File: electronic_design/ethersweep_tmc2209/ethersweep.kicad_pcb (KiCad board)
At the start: 2 copper layers, 79 x 38 mm, 111 parts, among them J1 AVR-ISP-6, J10 HR911105A, J12 USB_C_Receptacle_USB2.0, J2 Conn_01x02_Male, J3 Conn_01x04_Female, J4 Conn_01x03_Male, J5 Conn_01x03_Male, J6 Conn_01x06_Female, J7 Conn_01x06_Male, J8 AVR-ISP-6, J9 Conn_01x04_Female, SW1 SW_Push, U3 STM32F103C8Tx, U4 DD4012SA, U5 AS5600, U6 W5500, U7 TMC2209-LA, Y2 Crystal_25MHz, Y3 Crystal

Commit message: minor design changes
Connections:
- U3 pad 11: voltage_detect -> RST_ETHERNET
- U3 pad 19: RST_ETHERNET -> voltage_detect
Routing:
- net ETH_INT: track 45.0 -> 47.3 mm
- net voltage_detect: track 15.6 -> 13.7 mm
- net +3V3: track 248.8 -> 250.2 mm
- net rst: track 38.6 -> 39.8 mm
- net ESTOP: track 53.3 -> 52.6 mm
- net MOT_UART_RX: track 35.6 -> 34.8 mm
- net RST_ETHERNET: track 46.1 -> 46.7 mm
- net SCK: track 53.3 -> 53.9 mm
- net GND: vias 217 -> 252
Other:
- board text added: "ETHERSWEEP 2023-01-14"
- board text removed: "ETHERSWEEP 2023-01-10"

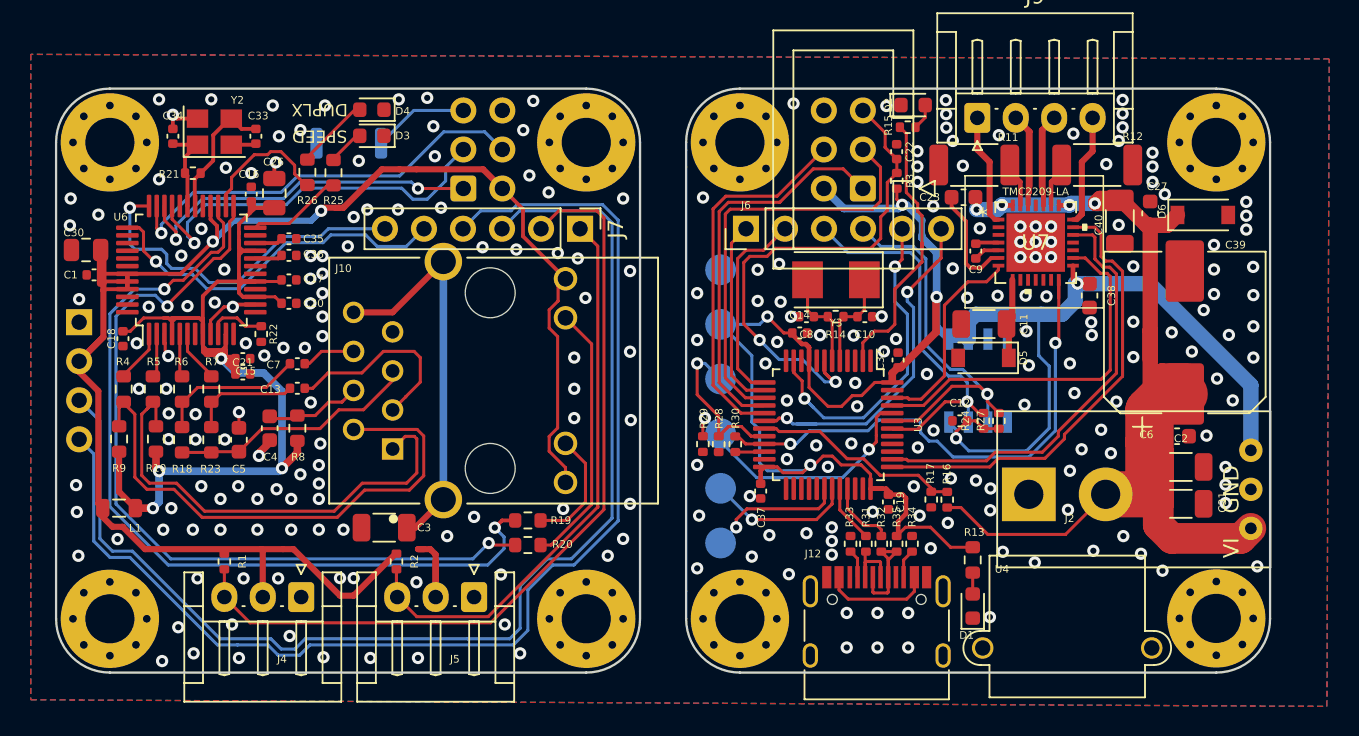
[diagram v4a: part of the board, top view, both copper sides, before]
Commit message: pcb design changes, reorganisation, JLC part number assignments, size corrections
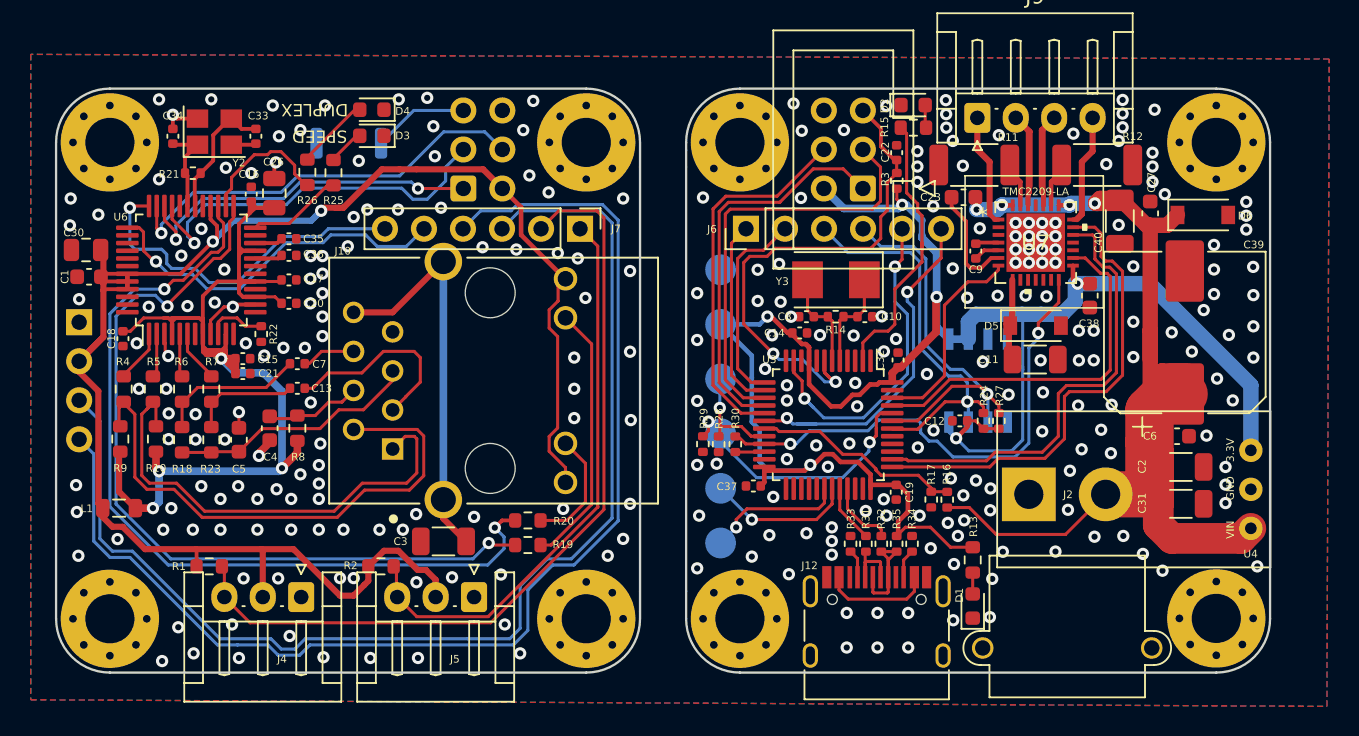
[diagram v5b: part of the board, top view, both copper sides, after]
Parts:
- C1: footprint Capacitor_SMD:C_0402_1005Metric -> Capacitor_SMD:C_0603_1608Metric
- R1, R15, R2: footprint Resistor_SMD:R_0402_1005Metric -> Resistor_SMD:R_0603_1608Metric
- moved C11 4.06 mm to (209.8, 44.3), turned to 0 degrees
- moved D5 3.98 mm to (209.8, 42.1), turned to 0 degrees
- moved C3 3.96 mm to (171.3, 56.2)
- moved R2 1.06 mm to (167.2, 57.8), turned to 0 degrees
- moved R1 1.03 mm to (156.1, 57.8), turned to 0 degrees
- moved C19 0.81 mm to (200.8, 53.0)
- moved C37 0.58 mm to (191.5, 52.6), turned to 180 degrees
- moved R15 0.37 mm to (201.9, 29.2)
- moved C1 0.35 mm to (148.2, 38.9)
- moved R9 0.08 mm to (150.3, 49.5)
- moved C22 0.07 mm to (200.8, 30.9)
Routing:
- net BOOT_1: track 11.3 -> 7.74 mm
- net +3V3: track 250.2 -> 248.3 mm
- net MOT_UART_RX: track 34.8 -> 33.1 mm
- net MOT_DIR: track 28.3 -> 29.8 mm
- net MOT_STANDBY: track 29.7 -> 31.1 mm
- net SCL: track 105.3 -> 104.8 mm
- net GND: vias 252 -> 278
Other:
- board text added: "3.3V"
- board text added: "5.5...28V"
- board text added: "BOOT_0"
- board text added: "BOOT_1"
- board text added: "DUPLEX"
- board text added: "ETHERSWEEP 2023-01-24 rev. 4.0.1 github.com/neumi/ethersweep"
- board text added: "GND"
- board text added: "MOTOR"
- board text added: "RX"
- board text added: "TX"
- board text added: "USB C"
- board text removed: "DUPLX"
- board text removed: "ETHERSWEEP 2023-01-14"
- board text removed: "rev. 4.0.1"

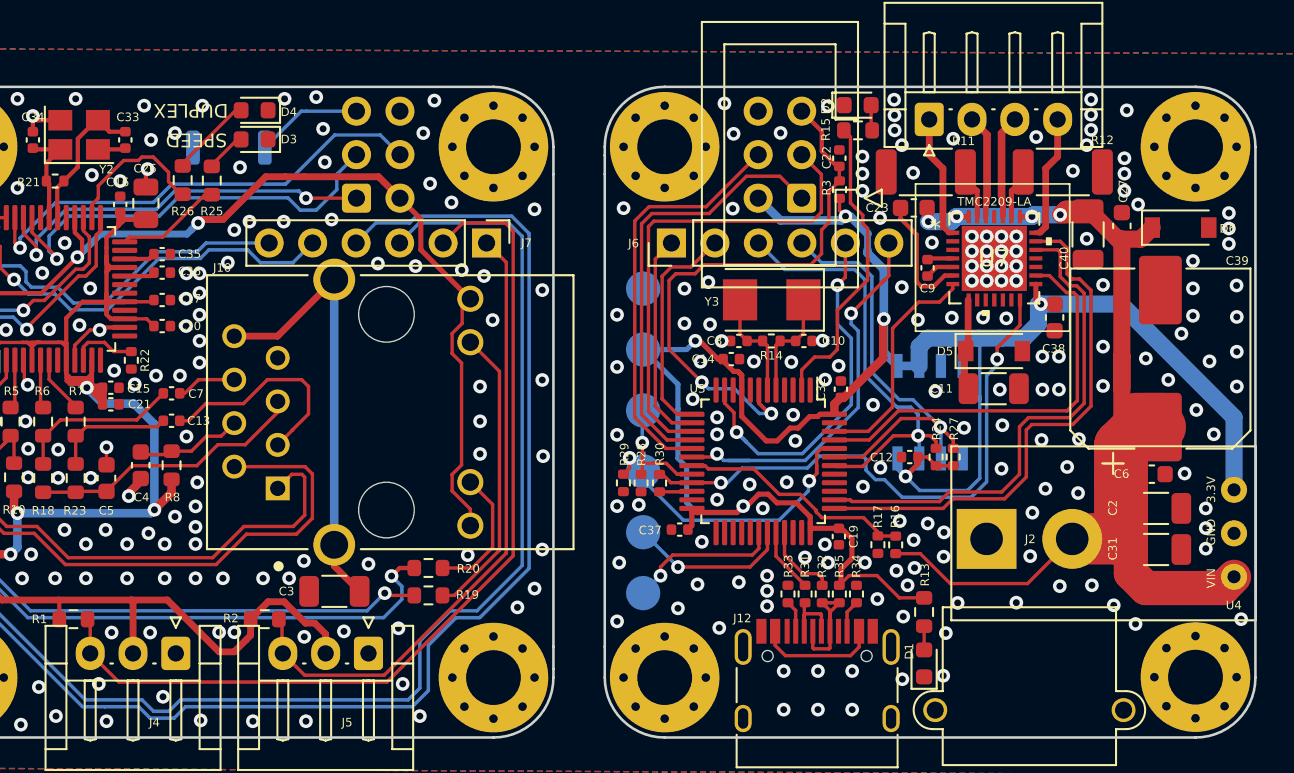
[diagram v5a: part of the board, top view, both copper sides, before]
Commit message: part assignments, minor part changes
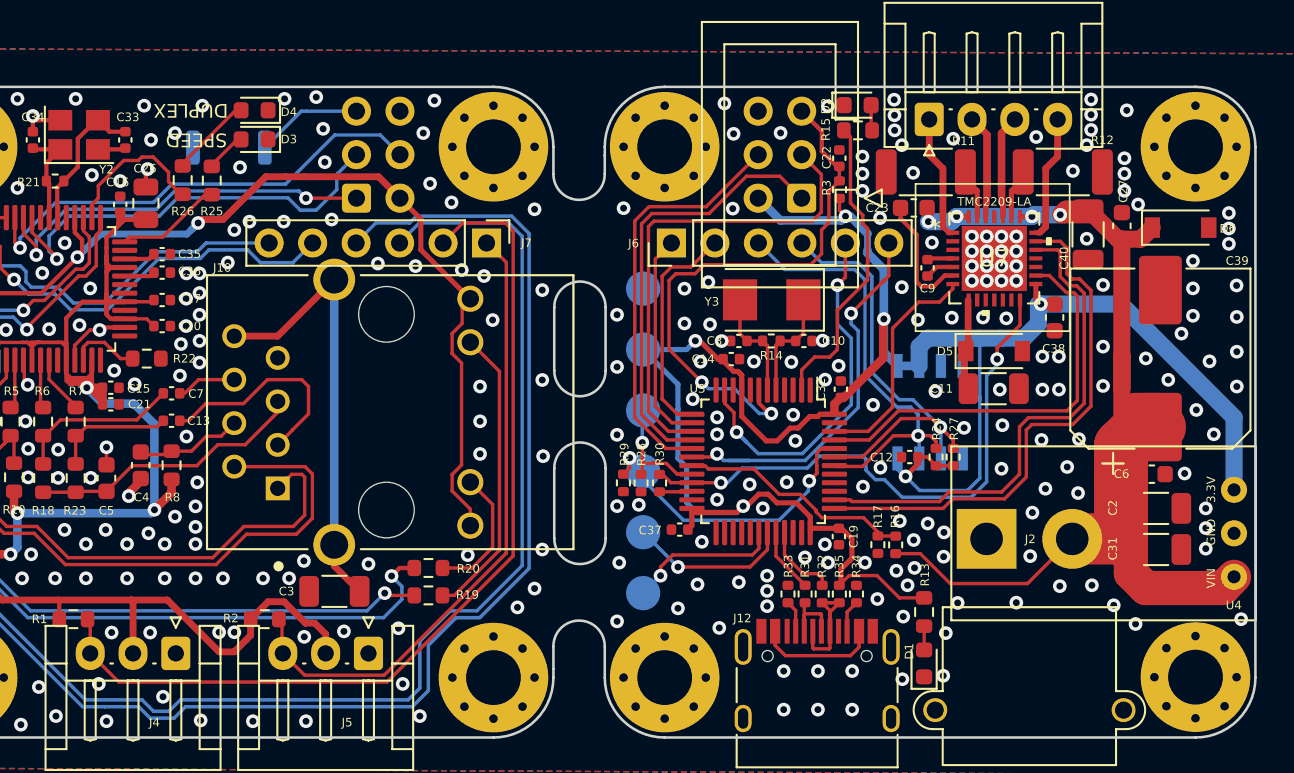
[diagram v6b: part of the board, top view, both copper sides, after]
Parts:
- R22: footprint Resistor_SMD:R_0402_1005Metric -> Resistor_SMD:R_0603_1608Metric
- moved R22 0.91 mm to (160.3, 42.6), turned to 180 degrees
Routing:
- net Net-(R22-Pad2): track 3.90 -> 4.47 mm
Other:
- outline, holes or cut-outs redrawn
